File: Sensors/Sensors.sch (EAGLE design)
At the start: 34 parts, among them J2 JST_CONNECTOR, J6 JST_CONNECTOR, J7 JST_CONNECTOR, J8 JST_CONNECTOR, J9 JST_CONNECTOR

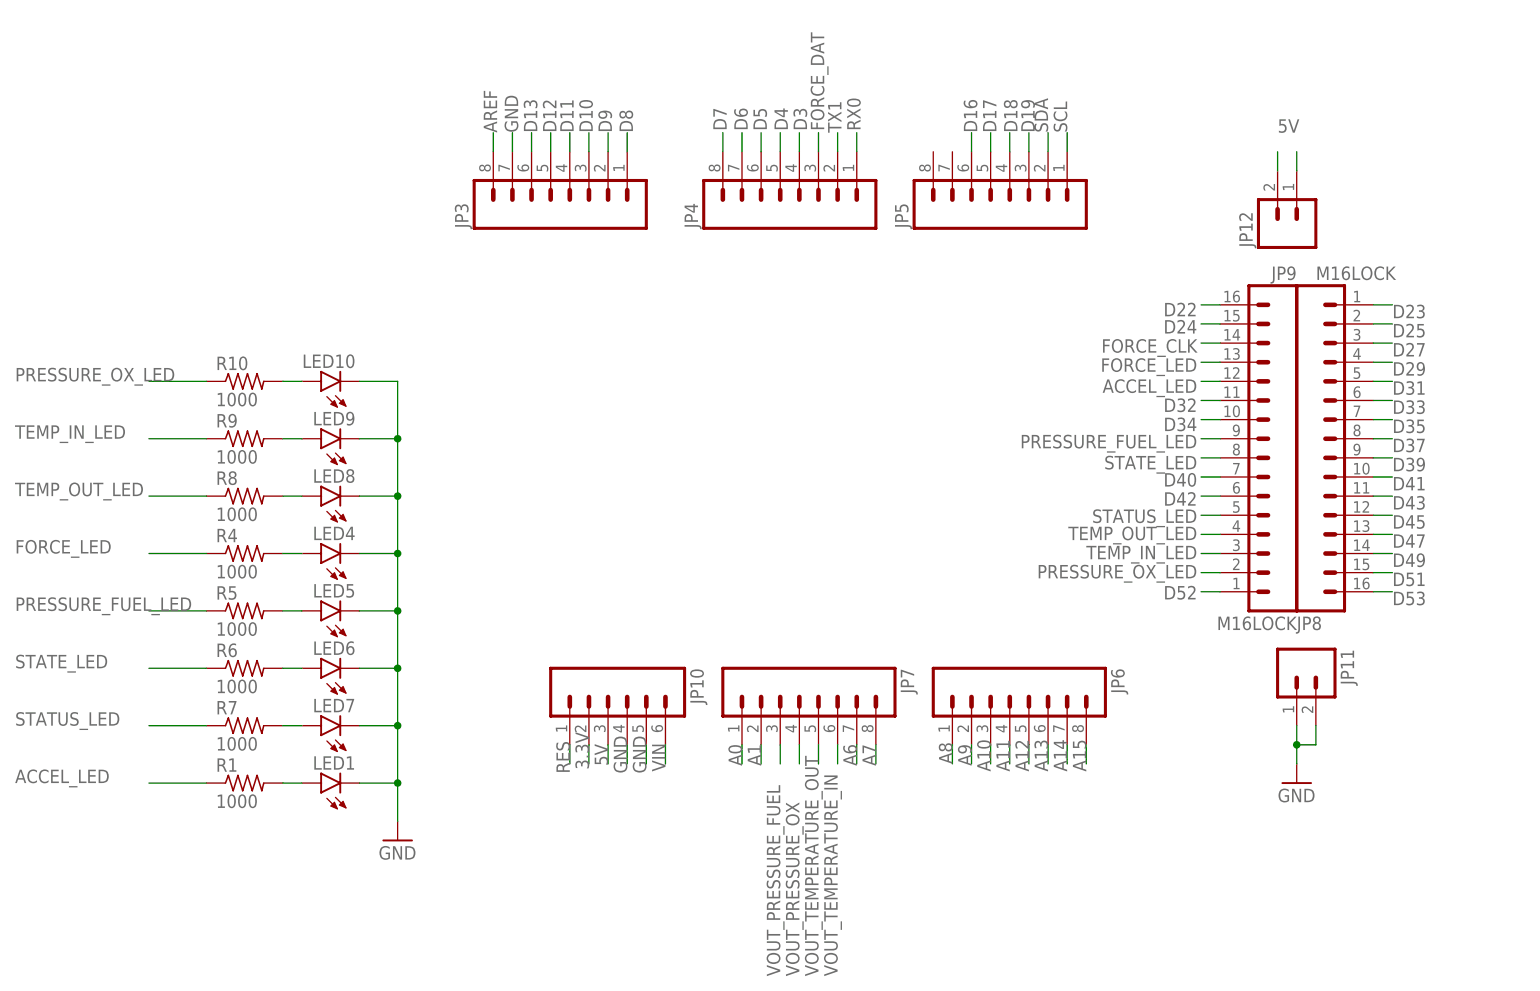
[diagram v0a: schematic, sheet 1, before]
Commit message: Redesign sensors PCB - remove LEDs and add additional components
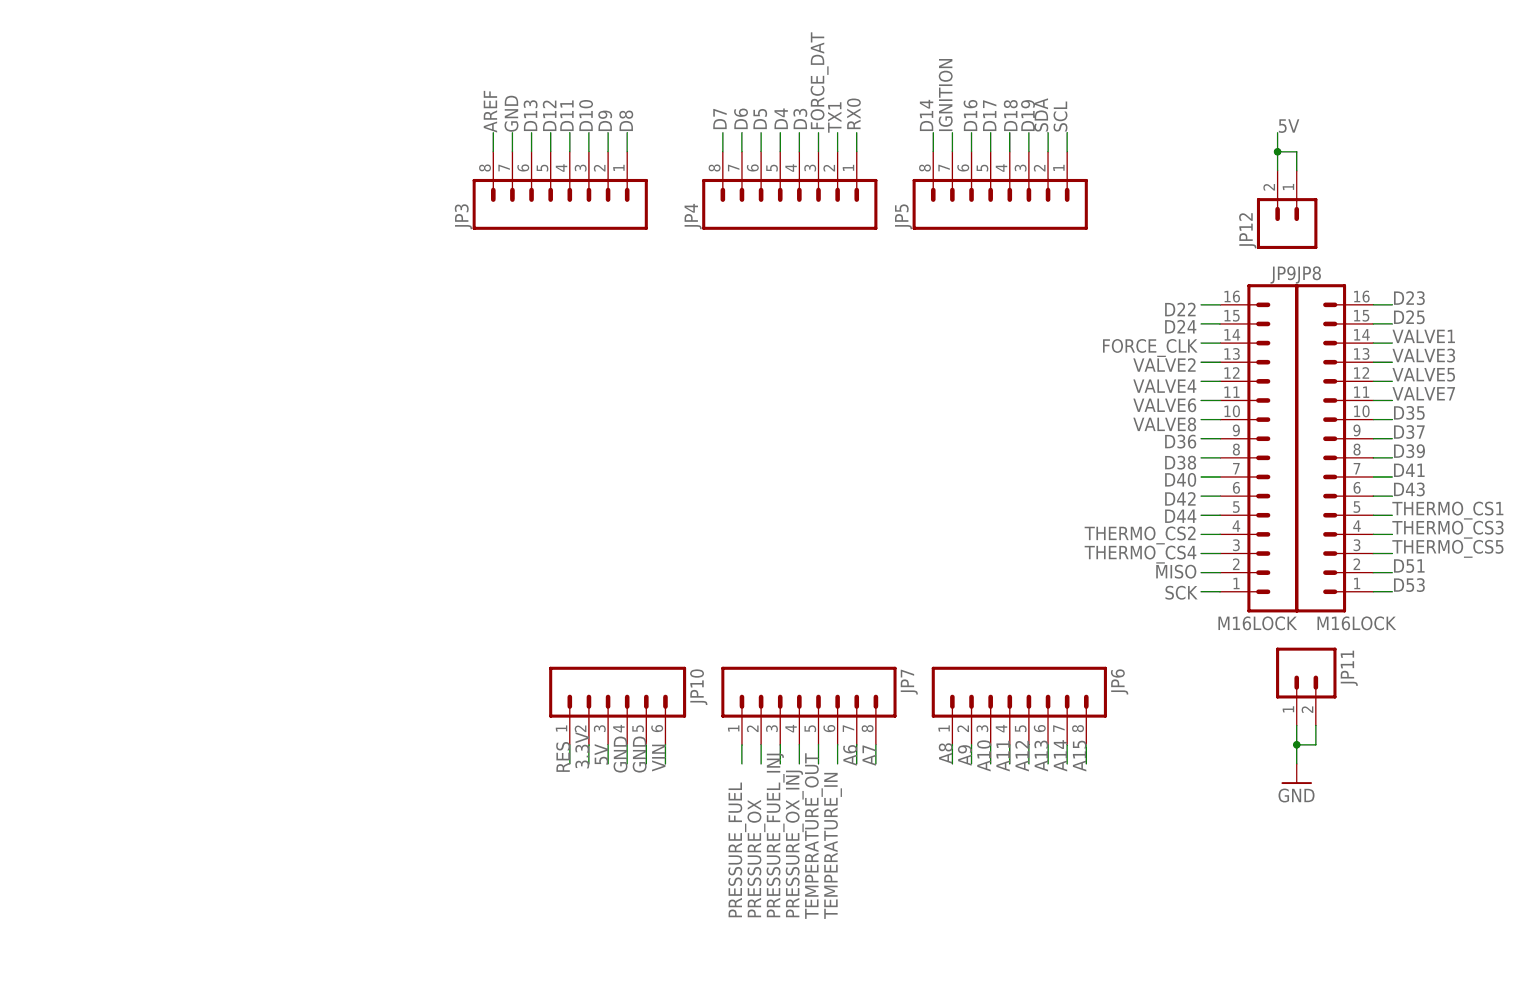
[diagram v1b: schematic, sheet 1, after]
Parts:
- removed LED1, LED10, LED4, LED5, LED6, LED7, LED8, LED9: (no value), led:LED3MM
- removed R1, R10, R4, R5, R6, R7, R8, R9: 1000, rcl:R-US_0204/7
- added J10, J11, J5: JST_CONNECTOR, LPRD_RELAY:JST_CONNECTOR
- added J12, J13, J14, J15, J16: (no value), SparkFun-Connectors:CONN_06SILK_FEMALE_PTH
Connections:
- net D32 renamed VALVE6
- net D34 renamed VALVE8
- net D45 renamed VALVE5
- net D47 renamed VALVE3
- net D49 renamed VALVE1
- net VOUT_TEMPERATURE_IN renamed TEMPERATURE_IN
- net VOUT_TEMPERATURE_OUT renamed TEMPERATURE_OUT
- removed net A0: JP7.1
- removed net A1: JP7.2
- removed net ACCEL_LED: JP9.12, R1.1
- removed net D27: JP8.3
- removed net D29: JP8.4
- removed net D31: JP8.5
- removed net D33: JP8.6
- removed net D52: JP9.1
- removed net FORCE_LED: JP9.13, R4.1
- removed net N$1: LED1.A, R1.2
- removed net N$15: LED8.A, R8.2
- removed net N$16: LED9.A, R9.2
- removed net N$23: LED10.A, R10.2
- removed net N$4: LED4.A, R4.2
- removed net N$5: LED5.A, R5.2
- removed net N$6: LED6.A, R6.2
- removed net N$7: LED7.A, R7.2
- removed net PRESSURE_FUEL_LED: JP9.9, R5.1
- removed net PRESSURE_OX_LED: JP9.2, R10.1
- removed net STATE_LED: JP9.8, R6.1
- removed net STATUS_LED: JP9.5, R7.1
- removed net TEMP_IN_LED: JP9.3, R9.1
- removed net TEMP_OUT_LED: JP9.4, R8.1
- removed net VOUT_PRESSURE_FUEL: J8.P2, JP7.3
- removed net VOUT_PRESSURE_OX: J9.P2, JP7.4
- new net D14: JP5.8
- new net D36: JP9.9
- new net D38: JP9.8
- new net D44: JP9.5
- new net IGNITION: JP5.7
- new net MISO: J12.3, J13.3, J14.3, J15.3, J16.3, JP9.2
- new net PRESSURE_FUEL: J8.P2, JP7.1
- new net PRESSURE_FUEL_INJ: J5.P2, JP7.3
- new net PRESSURE_OX: J9.P2, JP7.2
- new net PRESSURE_OX_INJ: J10.P2, JP7.4
- new net SCK: J12.1, J13.1, J14.1, J15.1, J16.1, JP9.1
- new net THERMO_CS1: J12.2, JP8.5
- new net THERMO_CS2: J13.2, JP9.4
- new net THERMO_CS3: J14.2, JP8.4
- new net THERMO_CS4: J15.2, JP9.3
- new net THERMO_CS5: J16.2, JP8.3
- new net VALVE2: JP9.13
- new net VALVE4: JP9.12
- new net VALVE7: JP8.11
- net 5V: now also J10.P3, J11.P3, J12.6, J13.6, J14.6, J15.6, J16.6, J5.P3
- net D23: now also JP8.16; no longer JP8.1
- net D25: now also JP8.15; no longer JP8.2
- net D35: now also JP8.10; no longer JP8.7
- net D37: now also JP8.9; no longer JP8.8
- net D39: now also JP8.8; no longer JP8.9
- net D41: now also JP8.7; no longer JP8.10
- net D43: now also JP8.6; no longer JP8.11
- net D51: now also JP8.2; no longer JP8.15
- net D53: now also JP8.1; no longer JP8.16
- net GND: now also J10.P4, J11.P4, J12.4, J13.4, J14.4, J15.4, J16.4, J5.P4; no longer LED1.C, LED10.C, LED4.C, LED5.C, LED6.C, LED7.C, LED8.C, LED9.C
- net SCL: now also J11.P2
- net SDA: now also J11.P1
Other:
- moved on the sheet: JP8

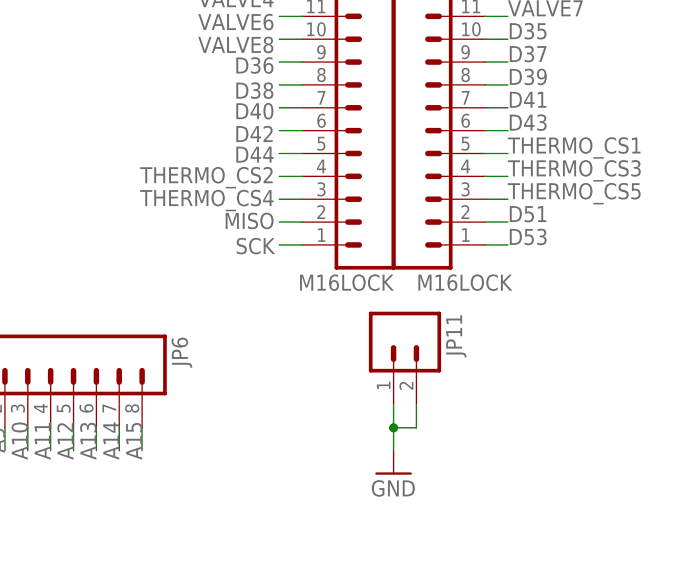
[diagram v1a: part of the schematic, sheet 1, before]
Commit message: Change header package to remove staggered pins
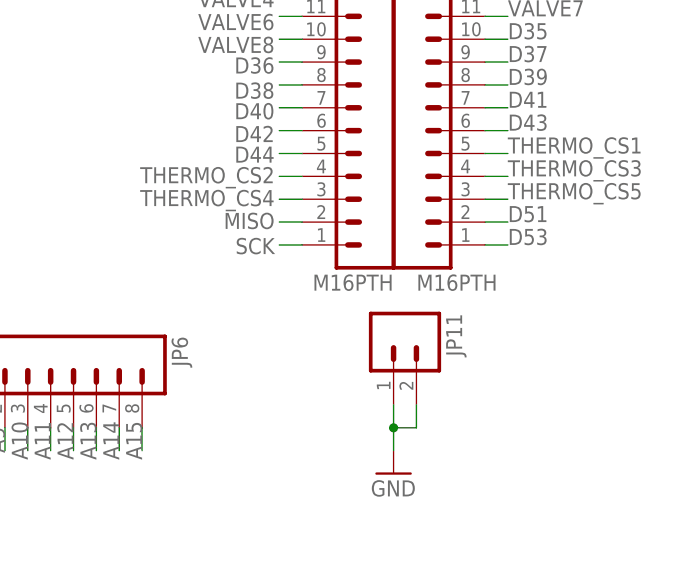
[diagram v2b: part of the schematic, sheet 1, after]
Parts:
- JP10: device SparkFun:M06LOCK -> SparkFun:M06SIP
- JP11, JP12: device SparkFun:M02LOCK -> SparkFun:M02PTH
- JP3, JP4, JP5, JP6, JP7: device SparkFun:M08LOCK -> SparkFun:M08
- JP8, JP9: value M16LOCK -> M16PTH; device SparkFun:M16LOCK -> SparkFun:M16PTH
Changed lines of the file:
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@@
 <grid distance="0.1" unitdist="inch" unit="inch" style="lines" multiple="1" display="no" altdistance="0.01" altunitdist="inch" altunit="inch"/>
 <layers>
-<layer number="1" name="Top" color="4" fill="1" visible="no" active="no"/>
-<layer number="2" name="Route2" color="1" fill="3" visible="no" active="no"/>
-<layer number="3" name="Route3" color="4" fill="3" visible="no" active="no"/>
-<layer number="4" name="Route4" color="1" fill="4" visible="no" active="no"/>
-<layer number="5" name="Route5" color="4" fill="4" visible="no" active="no"/>
-<layer number="6" name="Route6" color="1" fill="8" visible="no" active="no"/>
-<layer number="7" name="Route7" color="4" fill="8" visible="no" active="no"/>
-<layer number="8" name="Route8" color="1" fill="2" visible="no" active="no"/>
-<layer number="9" name="Route9" color="4" fill="2" visible="no" active="no"/>
-<layer number="10" name="Route10" color="1" fill="7" visible="no" active="no"/>
-<layer number="11" name="Route11" color="4" fill="7" visible="no" active="no"/>
-<layer number="12" name="Route12" color="1" fill="5" visible="no" active="no"/>
-<layer number="13" name="Route13" color="4" fill="5" visible="no" active="no"/>
-<layer number="14" name="Route14" color="1" fill="6" visible="no" active="no"/>
-<layer number="15" name="Route15" color="4" fill="6" visible="no" active="no"/>
-<layer number="16" name="Bottom" color="1" fill="1" visible="no" active="no"/>
-<layer number="17" name="Pads" color="2" fill="1" visible="no" active="no"/>
-<layer number="18" name="Vias" color="2" fill="1" visible="no" active="no"/>
-<layer number="19" name="Unrouted" color="6" fill="1" visible="no" active="no"/>
-<layer number="20" name="Dimension" color="15" fill="1" visible="no" active="no"/>
-<layer number="21" name="tPlace" color="16" fill="1" visible="no" active="no"/>
-<layer number="22" name="bPlace" color="14" fill="1" visible="no" active="no"/>
-<layer number="23" name="tOrigins" color="15" fill="1" visible="no" active="no"/>
-<layer number="24" name="bOrigins" color="15" fill="1" visible="no" active="no"/>
-<layer number="25" name="tNames" color="7" fill="1" visible="no" active="no"/>
-<layer number="26" name="bNames" color="7" fill="1" visible="no" active="no"/>
-<layer number="27" name="tValues" color="7" fill="1" visible="no" active="no"/>
-<layer number="28" name="bValues" color="7" fill="1" visible="no" active="no"/>
+<layer number="1" name="Top" color="4" fill="1" visible="yes" active="no"/>
+<layer number="2" name="Route2" color="1" fill="3" visible="yes" active="no"/>
+<layer number="3" name="Route3" color="4" fill="3" visible="yes" active="no"/>
+<layer number="4" name="Route4" color="1" fill="4" visible="yes" active="no"/>
+<layer number="5" name="Route5" color="4" fill="4" visible="yes" active="no"/>
+<layer number="6" name="Route6" color="1" fill="8" visible="yes" active="no"/>
+<layer number="7" name="Route7" color="4" fill="8" visible="yes" active="no"/>
+<layer number="8" name="Route8" color="1" fill="2" visible="yes" active="no"/>
+<layer number="9" name="Route9" color="4" fill="2" visible="yes" active="no"/>
+<layer number="10" name="Route10" color="1" fill="7" visible="yes" active="no"/>
+<layer number="11" name="Route11" color="4" fill="7" visible="yes" active="no"/>
+<layer number="12" name="Route12" color="1" fill="5" visible="yes" active="no"/>
+<layer number="13" name="Route13" color="4" fill="5" visible="yes" active="no"/>
+<layer number="14" name="Route14" color="1" fill="6" visible="yes" active="no"/>
+<layer number="15" name="Route15" color="4" fill="6" visible="yes" active="no"/>
+<layer number="16" name="Bottom" color="1" fill="1" visible="yes" active="no"/>
+<layer number="17" name="Pads" color="2" fill="1" visible="yes" active="no"/>
+<layer number="18" name="Vias" color="2" fill="1" visible="yes" active="no"/>
+<layer number="19" name="Unrouted" color="6" fill="1" visible="yes" active="no"/>
+<layer number="20" name="Dimension" color="15" fill="1" visible="yes" active="no"/>
+<layer number="21" name="tPlace" color="16" fill="1" visible="yes" active="no"/>
+<layer number="22" name="bPlace" color="14" fill="1" visible="yes" active="no"/>
+<layer number="23" name="tOrigins" color="15" fill="1" visible="yes" active="no"/>
+<layer number="24" name="bOrigins" color="15" fill="1" visible="yes" active="no"/>
+<layer number="25" name="tNames" color="7" fill="1" visible="yes" active="no"/>
+<layer number="26" name="bNames" color="7" fill="1" visible="yes" active="no"/>
+<layer number="27" name="tValues" color="7" fill="1" visible="yes" active="no"/>
+<layer number="28" name="bValues" color="7" fill="1" visible="yes" active="no"/>
 <layer number="29" name="tStop" color="7" fill="3" visible="no" active="no"/>
 <layer number="30" name="bStop" color="7" fill="6" visible="no" active="no"/>
@@
 <layer number="35" name="tGlue" color="7" fill="4" visible="no" active="no"/>
 <layer number="36" name="bGlue" color="7" fill="5" visible="no" active="no"/>
-<layer number="37" name="tTest" color="7" fill="1" visible="no" active="no"/>
-<layer number="38" name="bTest" color="7" fill="1" visible="no" active="no"/>
+<layer number="37" name="tTest" color="7" fill="1" visible="yes" active="no"/>
+<layer number="38" name="bTest" color="7" fill="1" visible="yes" active="no"/>
 <layer number="39" name="tKeepout" color="4" fill="11" visible="no" active="no"/>
 <layer number="40" name="bKeepout" color="1" fill="11" visible="no" active="no"/>
@@
 <layer number="44" name="Drills" color="7" fill="1" visible="no" active="no"/>
 <layer number="45" name="Holes" color="7" fill="1" visible="no" active="no"/>
-<layer number="46" name="Milling" color="3" fill="1" visible="no" active="no"/>
-<layer number="47" name="Measures" color="7" fill="1" visible="no" active="no"/>
-<layer number="48" name="Document" color="7" fill="1" visible="no" active="no"/>
-<layer number="49" name="Reference" color="7" fill="1" visible="no" active="no"/>
-<layer number="50" name="dxf" color="7" fill="1" visible="no" active="no"/>
-<layer number="51" name="tDocu" color="6" fill="1" visible="no" active="no"/>
-<layer number="52" name="bDocu" color="7" fill="1" visible="no" active="no"/>
-<layer number="53" name="tGND_GNDA" color="7" fill="9" visible="no" active="no"/>
-<layer number="54" name="bGND_GNDA" color="1" fill="9" visible="no" active="no"/>
-<layer number="56" name="wert" color="7" fill="1" visible="no" active="no"/>
-<layer number="57" name="tCAD" color="7" fill="1" visible="no" active="no"/>
-<layer number="59" name="tCarbon" color="7" fill="1" visible="no" active="no"/>
-<layer number="60" name="bCarbon" color="7" fill="1" visible="no" active="no"/>
+<layer number="46" name="Milling" color="3" fill="1" visible="yes" active="no"/>
+<layer number="47" name="Measures" color="7" fill="1" visible="yes" active="no"/>
+<layer number="48" name="Document" color="7" fill="1" visible="yes" active="no"/>
+<layer number="49" name="Reference" color="7" fill="1" visible="yes" active="no"/>
+<layer number="50" name="dxf" color="7" fill="1" visible="yes" active="no"/>
+<layer number="51" name="tDocu" color="6" fill="1" visible="yes" active="no"/>
+<layer number="52" name="bDocu" color="7" fill="1" visible="yes" active="no"/>
+<layer number="53" name="tGND_GNDA" color="7" fill="9" visible="yes" active="no"/>
+<layer number="54" name="bGND_GNDA" color="1" fill="9" visible="yes" active="no"/>
+<layer number="56" name="wert" color="7" fill="1" visible="yes" active="no"/>
+<layer number="57" name="tCAD" color="7" fill="1" visible="yes" active="no"/>
+<layer number="59" name="tCarbon" color="7" fill="1" visible="yes" active="no"/>
+<layer number="60" name="bCarbon" color="7" fill="1" visible="yes" active="no"/>
 <layer number="88" name="SimResults" color="9" fill="1" visible="yes" active="yes"/>
 <layer number="89" name="SimProbes" color="9" fill="1" visible="yes" active="yes"/>
@@
 <parts>
 <part name="FRAME1" library="SparkFun" deviceset="FRAME-LETTER" device=""/>
-<part name="JP3" library="SparkFun" deviceset="M08" device="LOCK"/>
-<part name="JP4" library="SparkFun" deviceset="M08" device="LOCK"/>
-<part name="JP5" library="SparkFun" deviceset="M08" device="LOCK"/>
-<part name="JP6" library="SparkFun" deviceset="M08" device="LOCK"/>
-<part name="JP7" library="SparkFun" deviceset="M08" device="LOCK"/>
-<part name="JP8" library="SparkFun" deviceset="M16" device="LOCK"/>
-<part name="JP9" library="SparkFun" deviceset="M16" device="LOCK"/>
-<part name="JP10" library="SparkFun" deviceset="M06" device="LOCK"/>
-<part name="JP11" library="SparkFun" deviceset="M02" device="LOCK"/>
-<part name="JP12" library="SparkFun" deviceset="M02" device="LOCK"/>
+<part name="JP3" library="SparkFun" deviceset="M08" device=""/>
+<part name="JP4" library="SparkFun" deviceset="M08" device=""/>
+<part name="JP5" library="SparkFun" deviceset="M08" device=""/>
+<part name="JP6" library="SparkFun" deviceset="M08" device=""/>
+<part name="JP7" library="SparkFun" deviceset="M08" device=""/>
+<part name="JP8" library="SparkFun" deviceset="M16" device="PTH" value="M16PTH"/>
+<part name="JP9" library="SparkFun" deviceset="M16" device="PTH" value="M16PTH"/>
+<part name="JP10" library="SparkFun" deviceset="M06" device="SIP"/>
+<part name="JP11" library="SparkFun" deviceset="M02" device="PTH"/>
+<part name="JP12" library="SparkFun" deviceset="M02" device="PTH"/>
 <part name="GND2" library="SparkFun" deviceset="GND" device=""/>
 <part name="J1" library="SparkFun-Connectors" library_urn="urn:adsk.eagle:library:513" deviceset="CONN_08" device="&quot;" package3d_urn="urn:adsk.eagle:package:38138/1"/>
